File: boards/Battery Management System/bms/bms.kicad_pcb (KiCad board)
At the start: 2 copper layers, 28 parts, among them J2 1986660-2, J3 B5B-XH-A, U1 BD48L32G, U2 BD48L32G, U3 BD48L32G, U4 BD48L32G, U5 SN74HC08DR

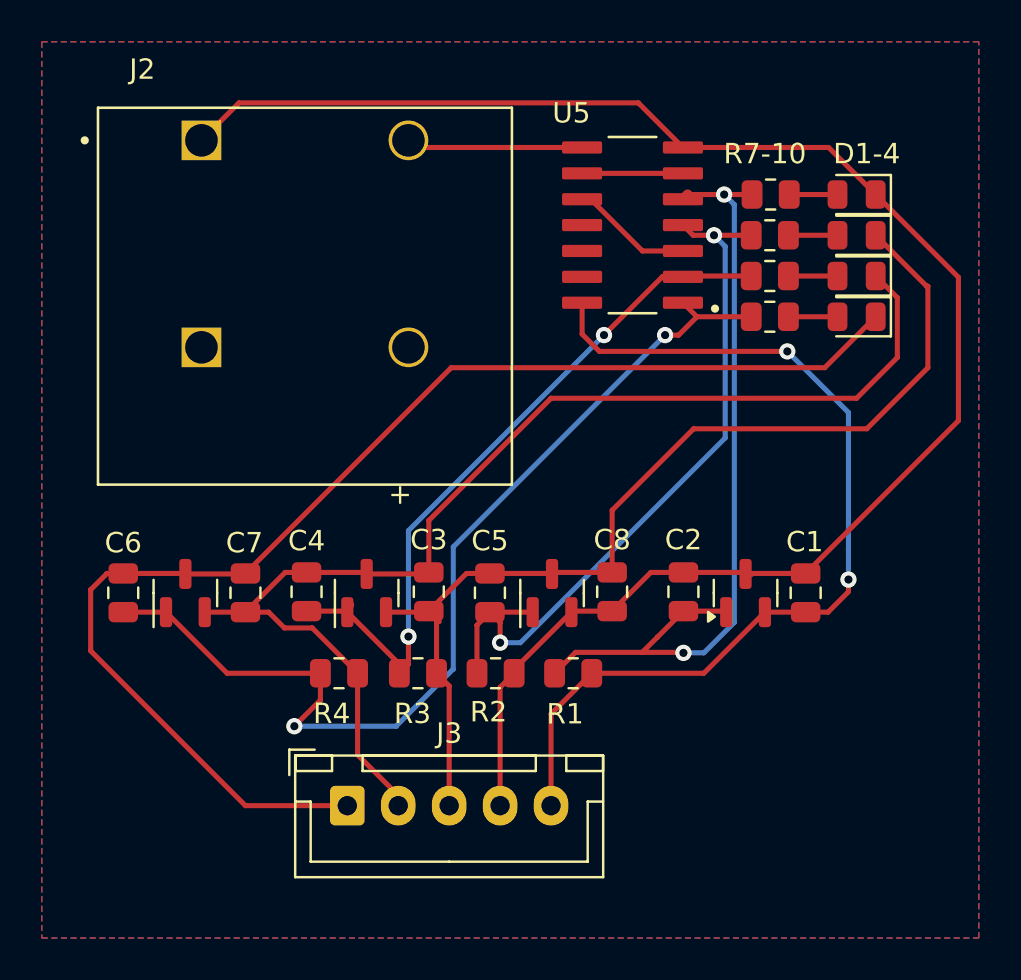
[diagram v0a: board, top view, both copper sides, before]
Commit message: Add edge cuts
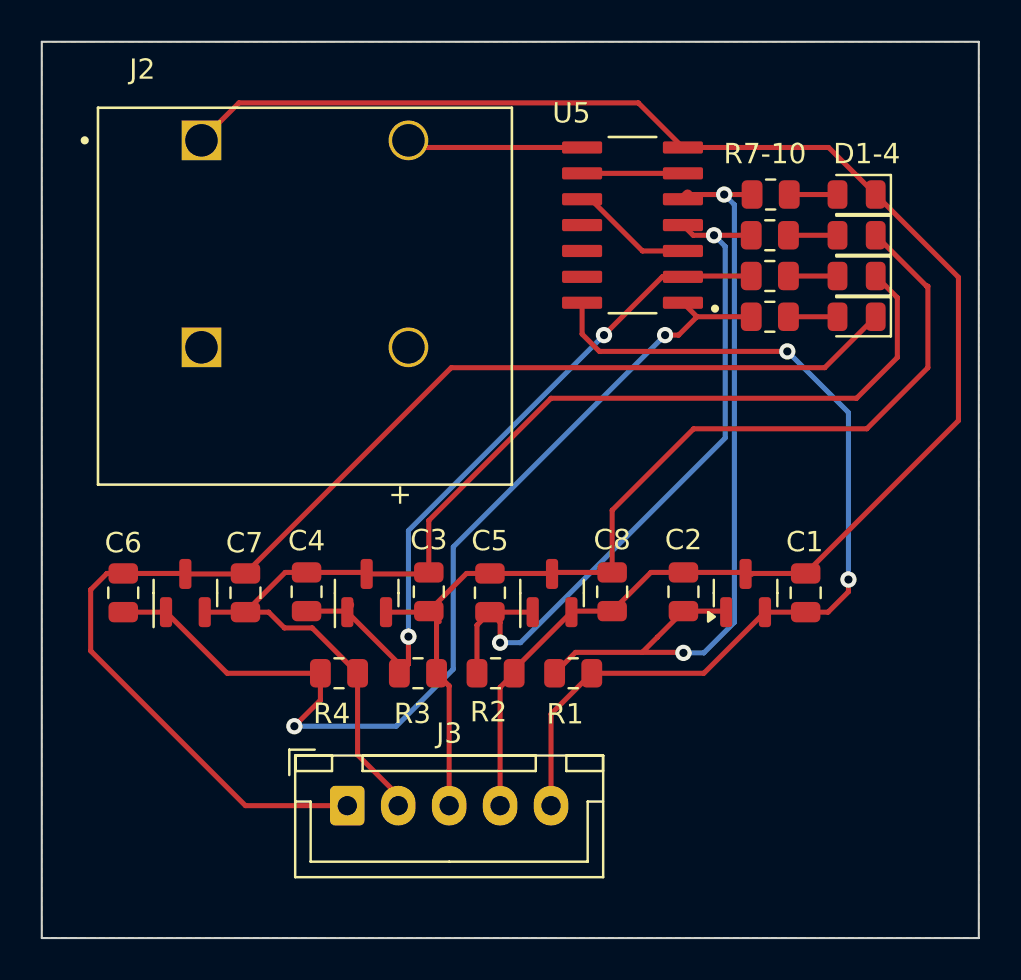
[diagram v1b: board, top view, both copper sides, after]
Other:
- board outline added: 46 x 44 mm
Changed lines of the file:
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@@
 		)
+	)
+	(gr_rect
+		(start 20 28)
+		(end 66 72)
+		(stroke
+			(width 0.1)
+			(type default)
+		)
+		(fill none)
+		(layer "Edge.Cuts")
 	)
 	(gr_text "+"
@@
 			(thermal_gap 0.5)
 			(thermal_bridge_width 0.5)
-		)
-		(polygon
-			(pts
-				(xy 20 28) (xy 20 72) (xy 66 72) (xy 66 28)
-			)
-		)
-	)
-	(zone
-		(net 0)
-		(net_name "")
-		(layer "Edge.Cuts")
-		(hatch edge 0.5)
-		(connect_pads
-			(clearance 0)
-		)
-		(min_thickness 0.25)
-		(filled_areas_thickness no)
-		(keepout
-			(tracks not_allowed)
-			(vias not_allowed)
-			(pads not_allowed)
-			(copperpour allowed)
-			(footprints allowed)
-		)
-		(fill
-			(thermal_gap 0.5)
-			(thermal_bridge_width 0.5)
